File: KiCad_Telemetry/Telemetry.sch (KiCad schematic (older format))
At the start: 42 parts, among them IC1 TCAN1044VDRQ1, J2 Conn_01x03, J3 PinHeader_01x02, J4 PinHeader_01x02, J7 DB9_Female, J8 USB Micro Connector, U1 NRF24L01_Breakout, U2 STM32F042C4T6, U3 TLV70033_SOT23-5, U4 MCP2518FDT, Y1 Crystal_GND24

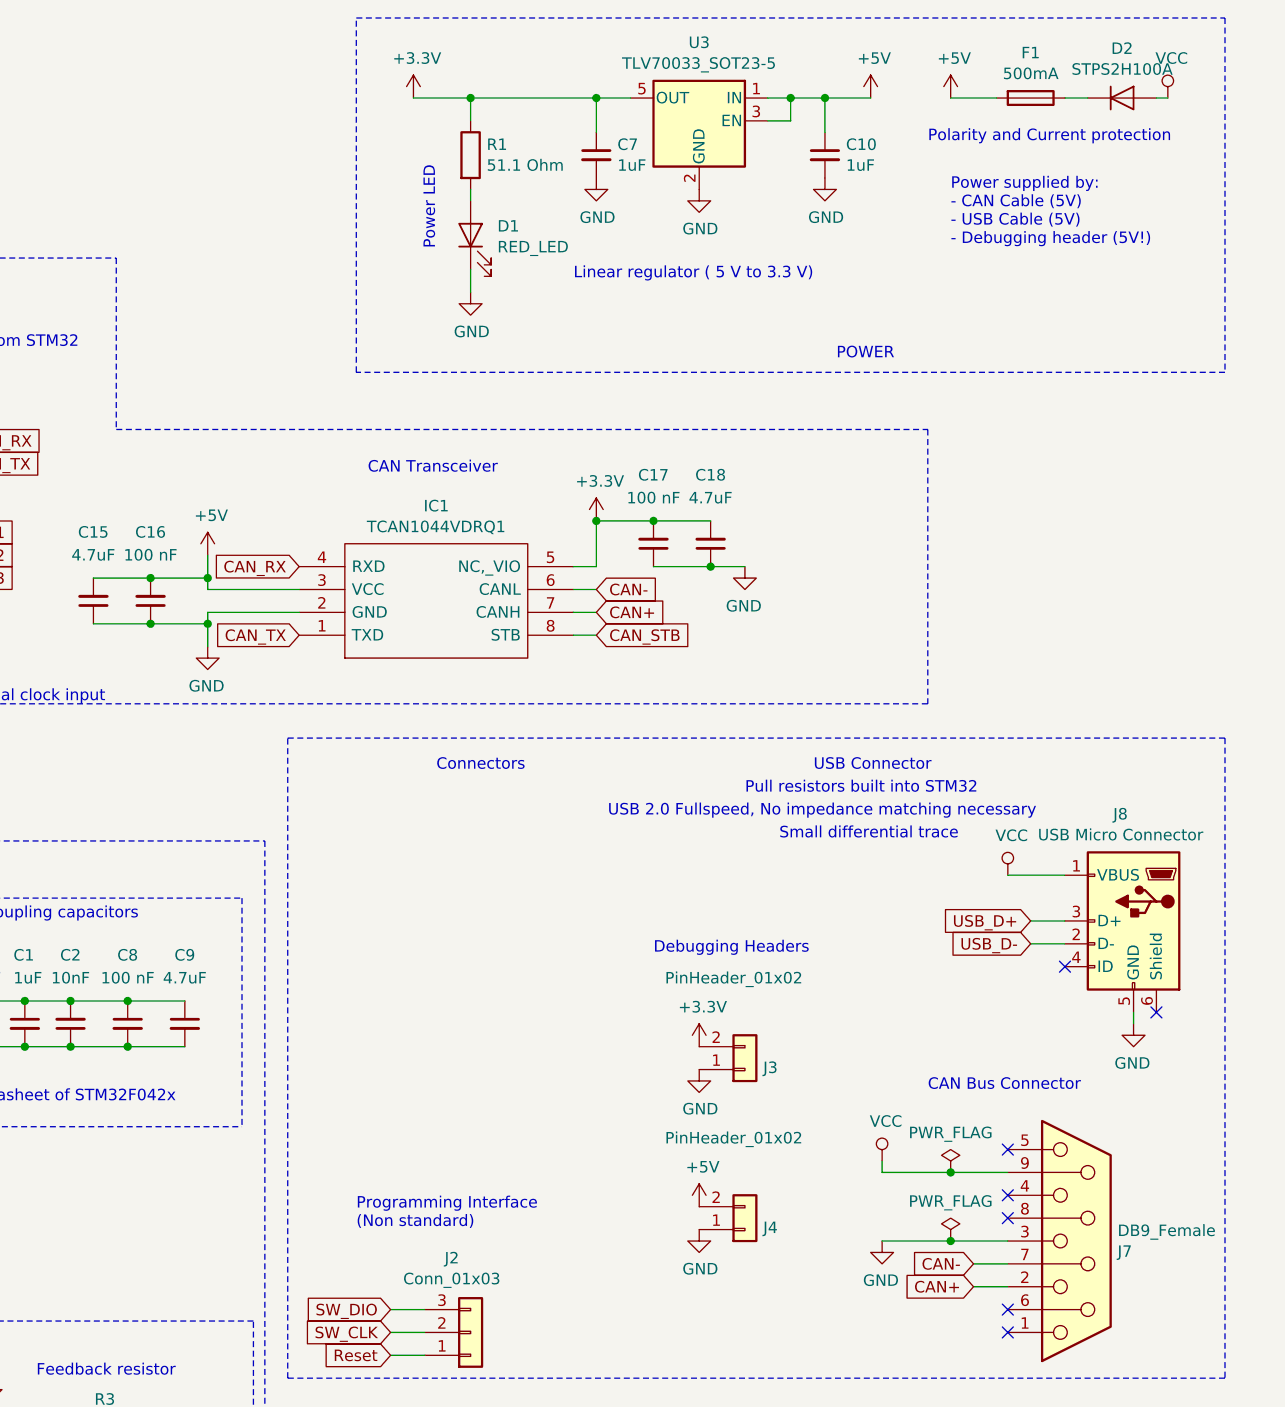
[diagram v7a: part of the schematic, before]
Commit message: Added Ferrite bead VBUS filtering Replaced LDO with component found on RS-Online (Same footprint, better parameters)
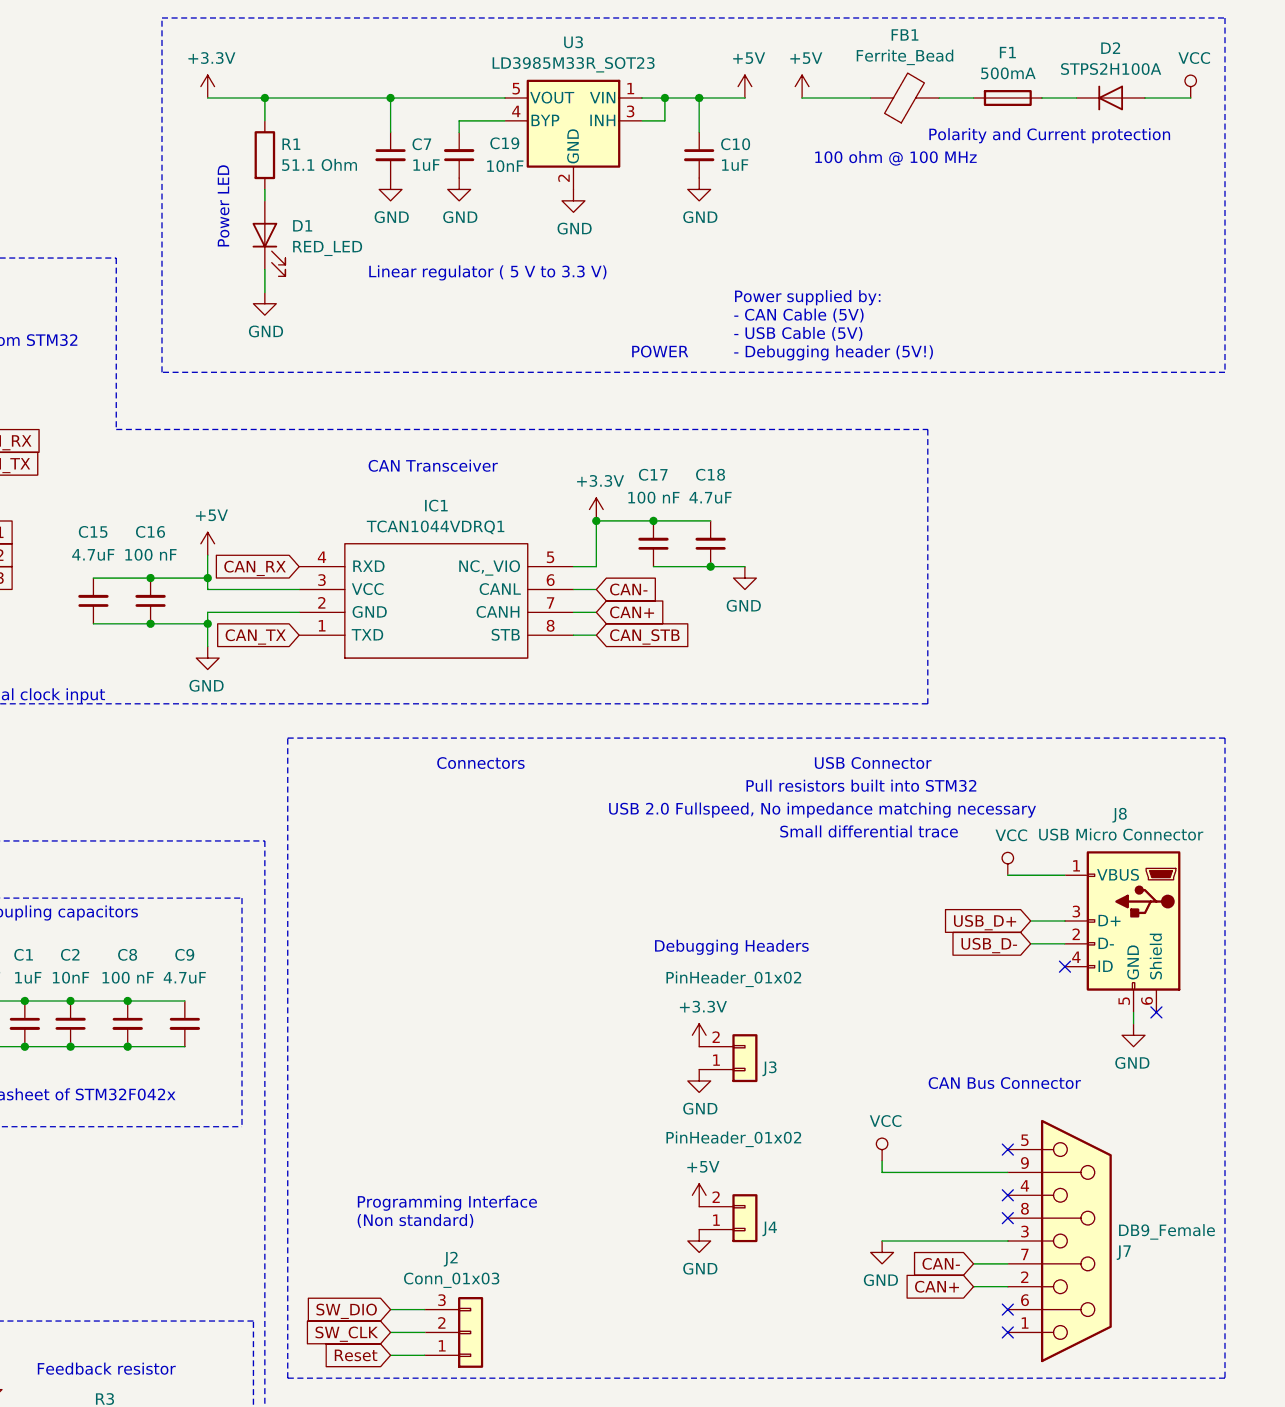
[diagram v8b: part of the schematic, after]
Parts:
- removed U3: TLV70033_SOT23-5, Package_TO_SOT_SMD:SOT-23-5, symbol Regulator_Linear:TLV70033_SOT23-5
- added C19: 10nF, Capacitor_SMD:C_0402_1005Metric, symbol Device:C_Small
- added FB1: Ferrite_Bead, Inductor_SMD:L_0603_1608Metric_Pad1.05x0.95mm_HandSolder, symbol Device:Ferrite_Bead
- added U3: LD3985M33R_SOT23, Package_TO_SOT_SMD:SOT-23-5, symbol Regulator_Linear:LD3985M33R_SOT23
- J8: footprint Connector_USB:USB_Micro-B_Molex-105017-0001 -> Connector_USB:USB_Micro-B_Molex_47346-0001
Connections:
- net +3V3: now also U3.5 (VOUT)
- net +5V: now also FB1.1, U3.1 (VIN), U3.3 (INH); no longer F1.2
- net GND: now also C19.1, U3.2 (GND)
- new net: F1.2, FB1.2
- new net: C19.2, U3.4 (BYP)
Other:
- note added: "100 ohm @ 100 MHz"
- moved on the sheet: C10, C7, D1, D2, F1, R1
